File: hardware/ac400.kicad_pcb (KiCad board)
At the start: 2 copper layers, 105.4 x 76.2 mm, 72 parts, among them J1 AVR-ISP-10, J2 LOW OUT, J3 MID OUT, J4 HIGH OUT, J5 COMMON OUT, J6 COMMON IN, J7 LINE IN, J8 3.3V IN, K1 SRD-03VDC-SL-C, K2 SRD-03VDC-SL-C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

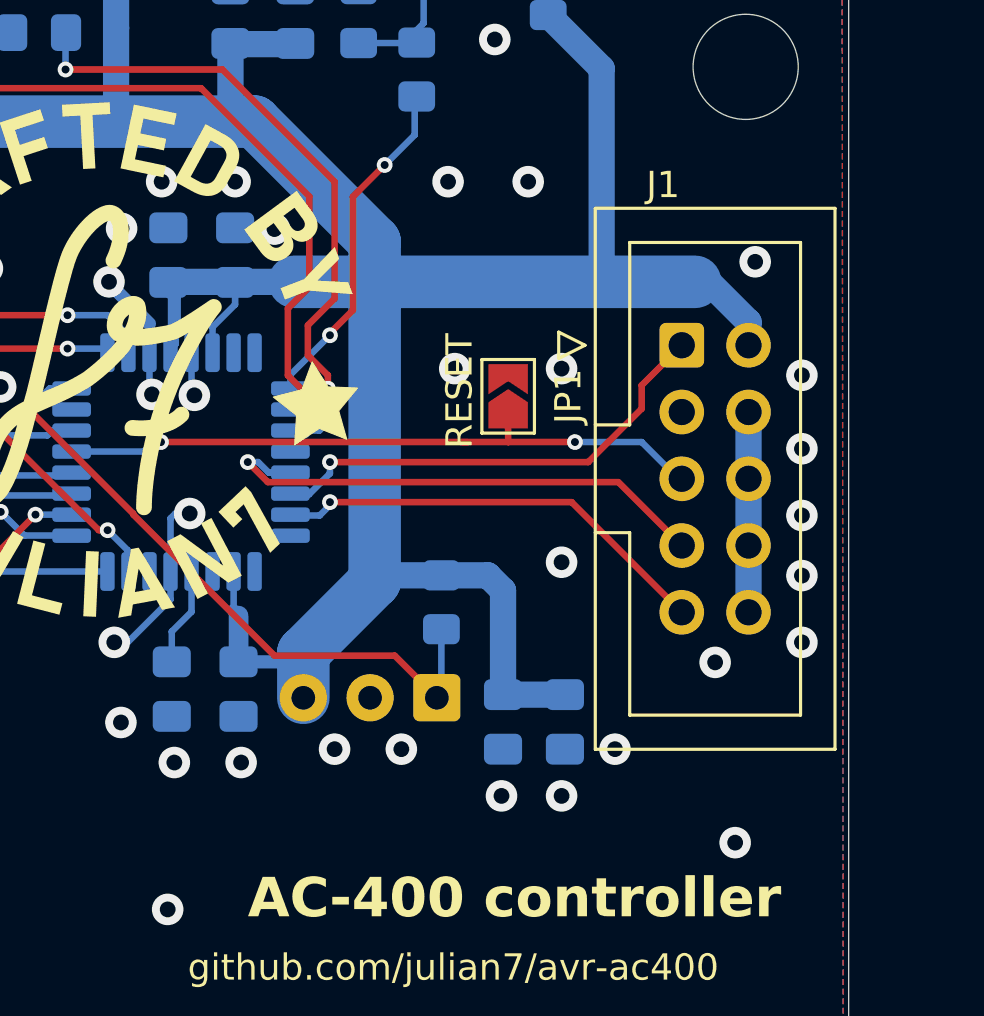
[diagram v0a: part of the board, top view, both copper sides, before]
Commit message: Replace MCU, fix SPI pins and footprint
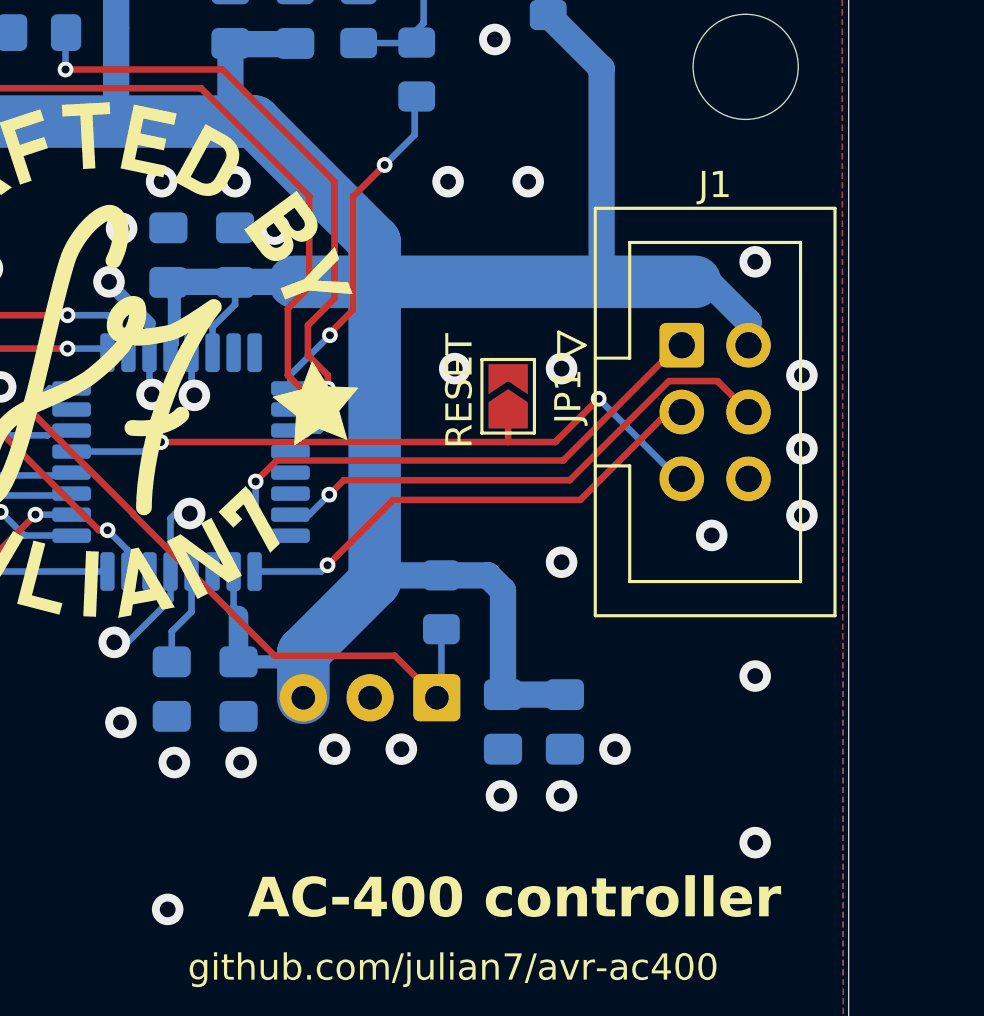
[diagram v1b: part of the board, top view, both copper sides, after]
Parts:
- J1: value AVR-ISP-10 -> AVR-ISP-6; footprint Connector_IDC:IDC-Header_2x05_P2.54mm_Vertical -> Connector_IDC:IDC-Header_2x03_P2.54mm_Vertical
- R3, R6, R9: value 2.2 0.25W -> 2.2
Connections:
- J1 pad 1: MOSI -> MISO
- J1 pad 3: unconnected-(J1-NC-Pad3) -> SCK
- J1 pad 4: GND -> MOSI
- U1 pad 13: SCK -> unconnected-(U1-PB1-Pad13)
- U1 pad 14: MOSI -> unconnected-(U1-PB2-Pad14)
- U1 pad 15: MISO -> MOSI
- U1 pad 16: unconnected-(U1-PB4-Pad16) -> MISO
- U1 pad 17: unconnected-(U1-PB5-Pad17) -> SCK
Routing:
- net GND: track 25.2 -> 17.5 mm, vias 107 -> 106
- net MISO: track 16.9 -> 21.3 mm
- net MOSI: track 18.0 -> 20.0 mm
- net RESET: track 25.2 -> 26.3 mm
- net SCK: track 19.6 -> 18.8 mm

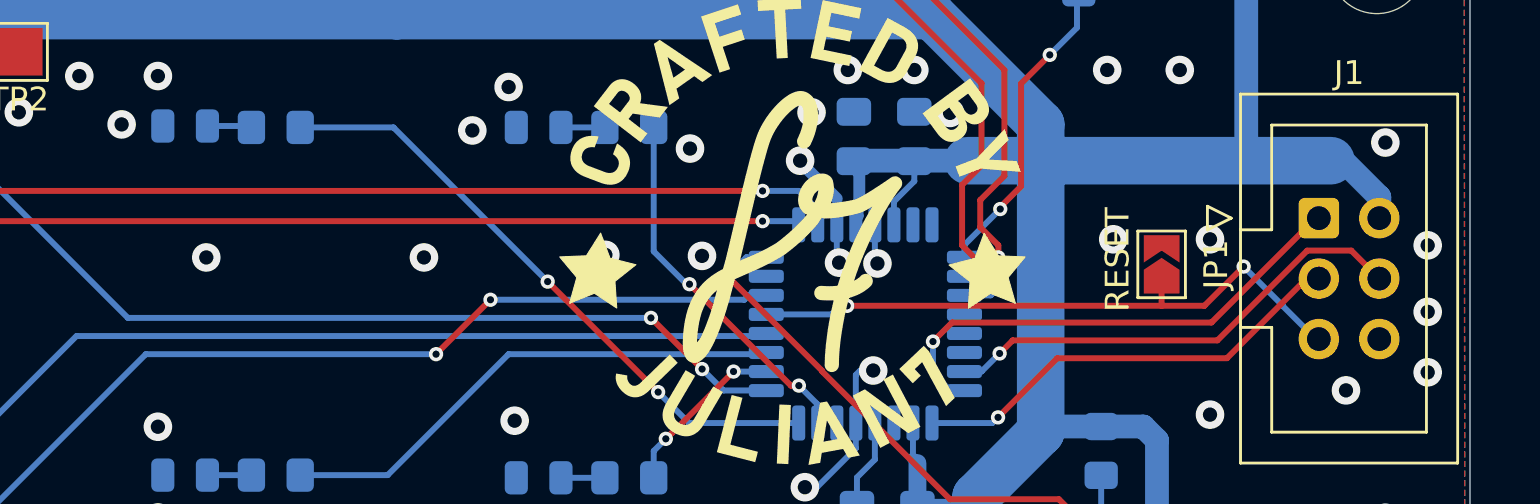
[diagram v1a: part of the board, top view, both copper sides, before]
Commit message: update design to KiCad 10.0 version
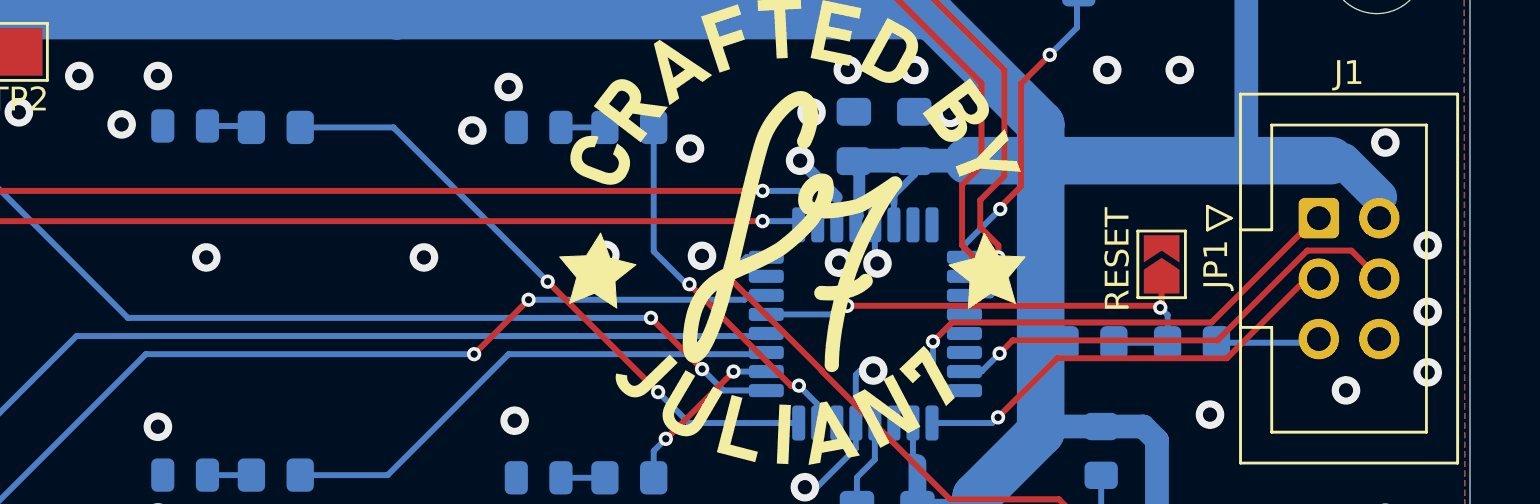
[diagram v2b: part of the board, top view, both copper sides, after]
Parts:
- added R19: 10k, PCM_Resistor_SMD_AKL:R_0805_2012Metric_Pad1.15x1.40mm_HandSolder, B.Cu at (170.7, 111.9)
- added R20: 1k, PCM_Resistor_SMD_AKL:R_0805_2012Metric_Pad1.15x1.40mm_HandSolder, B.Cu at (175.0, 111.9)
- U1: value ATmega88PA-A -> ATmega328P-A
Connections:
- J1 pad 5: RESET -> Net-(J1-~{RST})
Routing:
- net Net-(J1-~{RST}): track 0.00 -> 4.37 mm
- net RESET: track 26.3 -> 22.0 mm
- net GND: track 17.5 -> 16.0 mm, vias 106 -> 104
